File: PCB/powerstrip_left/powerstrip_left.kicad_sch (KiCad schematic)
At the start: 0 parts

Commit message: Stripe PCB's
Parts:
- added C1, C12, C13, C2: 100n, Capacitor_SMD:C_0201_0603Metric_Pad0.64x0.40mm_HandSolder, symbol Device:C
- added C10, C11, C3, C4, C5, C6, C7, C8, C9: C_Polarized, Capacitor_THT:CP_Radial_D5.0mm_P2.50mm, symbol Device:C_Polarized
- added C14: 1u, Capacitor_SMD:C_1206_3216Metric_Pad1.33x1.80mm_HandSolder, symbol Device:C
- added C15: 10u Tantal, Capacitor_SMD:C_1206_3216Metric_Pad1.33x1.80mm_HandSolder, symbol Device:C
- added IC1: PCA9685PW_Q900,118, Power_Strip_Library:SOP65P640X110-28N, symbol Power_Strip_Library:PCA9685PW_Q900,118
- added J1: XT60PW-M, Power_Strip_Library:AMASS_XT60PW-M, symbol Power_Strip_Library:XT60PW-M
- added J2, J3, J4: Conn_01x06_Pin, Connector_PinHeader_2.54mm:PinHeader_1x06_P2.54mm_Vertical, symbol Connector:Conn_01x06_Pin
- added J5, J6, J7: Conn_01x03_Pin, Connector_PinHeader_2.54mm:PinHeader_1x03_P2.54mm_Vertical, symbol Connector:Conn_01x03_Pin
- added J8: Conn_01x08_Pin, Connector_FFC-FPC:Amphenol_F32Q-1A7x1-11008_1x08-1MP_P0.5mm_Horizontal, symbol Connector:Conn_01x08_Pin
- added J9: Conn_01x02_Pin, Connector_JST:JST_XH_B2B-XH-AM_1x02_P2.50mm_Vertical, symbol Connector:Conn_01x02_Pin
- added U1: MUX508IDR, Power_Strip_Library:SOIC127P600X175-16N, symbol Power_Strip_Library:MUX508IDR
- added U2: INA181, Package_TO_SOT_SMD:SOT-23-6, symbol Amplifier_Current:INA181
- added U3: LT1117CST-3.3, PCM_Package_TO_SOT_SMD_AKL:SOT-223-3_TabPin2, symbol PCM_Voltage_Regulator_AKL:LT1117CST-3.3
- added shunt_01, shunt_2, shunt_3, shunt_4, shunt_5, shunt_6, shunt_7, shunt_8: R0.005, Resistor_SMD:R_0201_0603Metric_Pad0.64x0.40mm_HandSolder, symbol Device:R
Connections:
- new net: C1.1, U1.8 (D), U2.3 (+)
- new net 3.3V: C12.2, C13.1, C15.1, C2.1, IC1.28 (VDD), U1.13 (VDD), U2.6 (V+), U3.2 (OUT)
- new net A0: J8.4 (Pin_4), U1.1 (A0)
- new net A1: J8.3 (Pin_3), U1.16 (A1)
- new net A2: J8.2 (Pin_2), U1.15 (A2)
- new net ADC INPUT: J8.8 (Pin_8), U2.1
- new net GND: C1.2, C10.2, C11.2, C12.1, C13.2, C14.2, C15.2, C2.2, C3.2, C4.2, C5.2, C6.2, C7.2, C8.2, C9.2, IC1.1 (A0), IC1.14 (VSS), IC1.2 (A1), IC1.24 (A5), IC1.3 (A2), IC1.4 (A3), IC1.5 (A4), J1.2 (-), J2.2 (Pin_2), J8.1 (Pin_1), J9.1 (Pin_1), U1.14 (GND), U1.2 (EN), U1.3 (VSS), U2.2 (GND), U2.4 (-), U2.5 (REF), U3.1, shunt_01.2, shunt_2.2, shunt_3.2, shunt_4.2, shunt_5.2, shunt_6.2, shunt_7.2, shunt_8.2
- new net GND_SERVO1: J5.1 (Pin_1), U1.4 (S1), shunt_01.1
- new net GND_SERVO2: J5.2 (Pin_2), U1.5 (S2), shunt_2.1
- new net GND_SERVO3: J5.3 (Pin_3), U1.6 (S3), shunt_3.1
- new net GND_SERVO4: J2.1 (Pin_1), U1.7 (S4), shunt_4.1
- new net GND_SERVO6: J2.3 (Pin_3), U1.12 (S5), shunt_5.1
- new net GND_SERVO7: J2.4 (Pin_4), U1.11 (S6), shunt_6.1
- new net GND_SERVO8: J2.5 (Pin_5), U1.10 (S7), shunt_7.1
- new net GND_SERVO9: J2.6 (Pin_6), U1.9 (S8), shunt_8.1
- new net PWM_SERVO1: IC1.6 (LED0), J7.1 (Pin_1)
- new net PWM_SERVO2: IC1.7 (LED1), J7.2 (Pin_2)
- new net PWM_SERVO3: IC1.8 (LED2), J7.3 (Pin_3)
- new net PWM_SERVO4: IC1.9 (LED3), J4.1 (Pin_1)
- new net PWM_SERVO5: IC1.10 (LED4), J4.2 (Pin_2)
- new net PWM_SERVO6: IC1.11 (LED5), J4.3 (Pin_3)
- new net PWM_SERVO7: IC1.12 (LED6), J4.4 (Pin_4)
- new net PWM_SERVO8: IC1.13 (LED7), J4.5 (Pin_5)
- new net PWM_SERVO9: IC1.15 (LED8), J4.6 (Pin_6)
- new net SCL: IC1.26 (SCL), J8.6 (Pin_6)
- new net SDA: IC1.27 (SDA), J8.5 (Pin_5)
- new net VCC: C10.1, C11.1, C14.1, C3.1, C4.1, C5.1, C6.1, C7.1, C8.1, C9.1, J1.1 (+), J3.1 (Pin_1), J3.2 (Pin_2), J3.3 (Pin_3), J3.4 (Pin_4), J3.5 (Pin_5), J3.6 (Pin_6), J6.1 (Pin_1), J6.2 (Pin_2), J6.3 (Pin_3), J9.2 (Pin_2), U3.3 (IN)
- new net ¬EN: IC1.23 (~{OE}), J8.7 (Pin_7)
- no-connect marks 0 -> 8

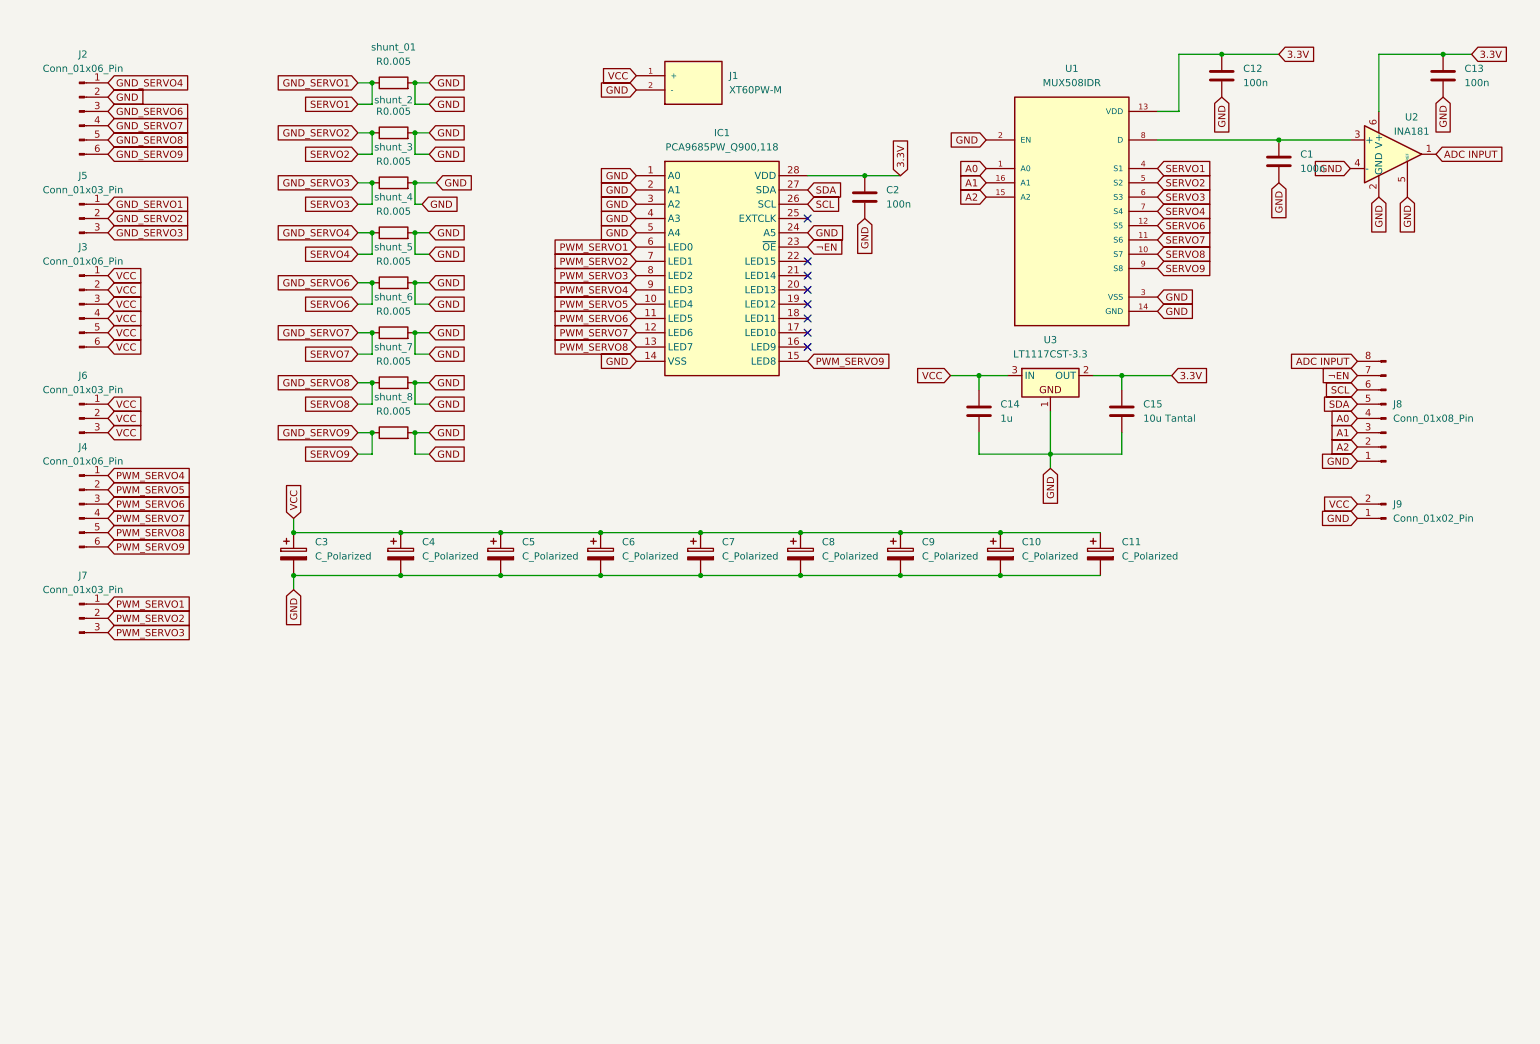
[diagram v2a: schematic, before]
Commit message: Stop tracking renders folder & final Powerstrip and Mainboard PCB
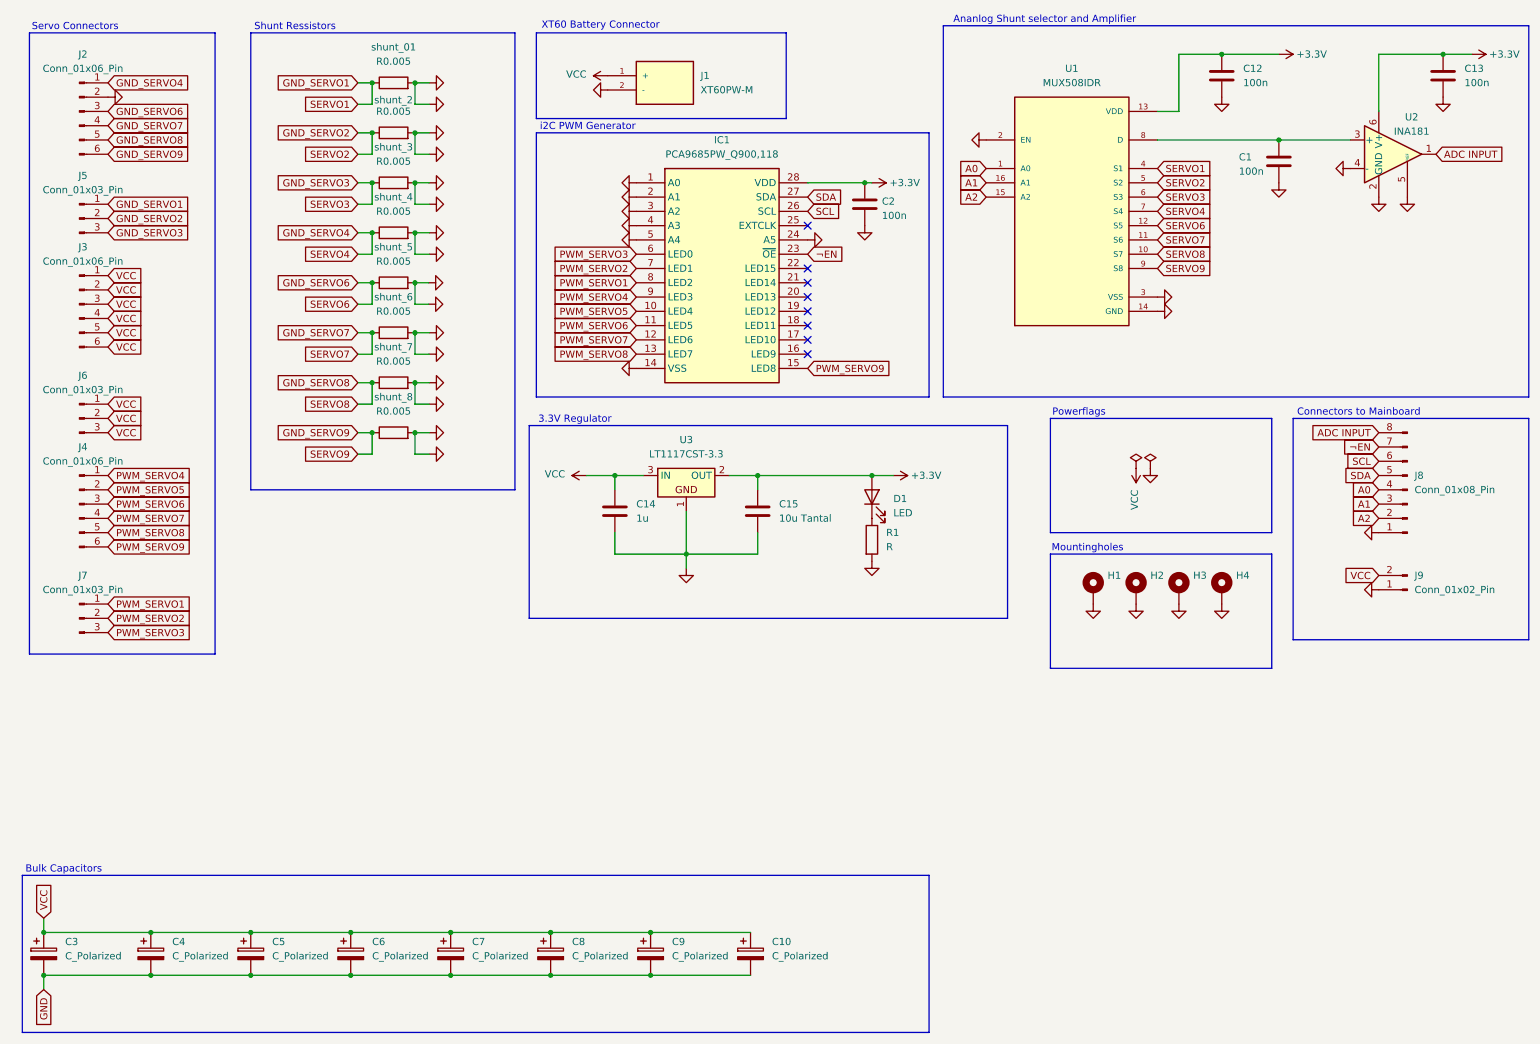
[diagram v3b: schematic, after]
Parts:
- removed C11: C_Polarized, Capacitor_THT:CP_Radial_D5.0mm_P2.50mm, symbol Device:C_Polarized
- added D1: LED, Power_Strip_Library:LEDC1608X70N, symbol Device:LED
- added H1, H2, H3, H4: MountingHole_Pad, MountingHole:MountingHole_3.5mm_Pad_Via, symbol Mechanical:MountingHole_Pad
- added R1: R, Resistor_SMD:R_0402_1005Metric_Pad0.72x0.64mm_HandSolder, symbol Device:R
- C1, C12, C13, C2: footprint Capacitor_SMD:C_0201_0603Metric_Pad0.64x0.40mm_HandSolder -> Capacitor_SMD:C_0402_1005Metric_Pad0.74x0.62mm_HandSolder
- J8: footprint Connector_FFC-FPC:Amphenol_F32Q-1A7x1-11008_1x08-1MP_P0.5mm_Horizontal -> Power_Strip_Library:17352658
- U3: footprint PCM_Package_TO_SOT_SMD_AKL:SOT-223-3_TabPin2 -> Power_Strip_Library:SOT230P700X180-4N
- shunt_01, shunt_2, shunt_3, shunt_4, shunt_5, shunt_6, shunt_7, shunt_8: footprint Resistor_SMD:R_0201_0603Metric_Pad0.64x0.40mm_HandSolder -> Resistor_SMD:R_1206_3216Metric_Pad1.30x1.75mm_HandSolder
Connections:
- net GND: now also H1.1, H2.1, H3.1, H4.1, R1.2
- net PWM_SERVO1: now also IC1.8 (LED2); no longer IC1.6 (LED0)
- net PWM_SERVO3: now also IC1.6 (LED0); no longer IC1.8 (LED2)
- net 3.3V renamed +3.3V
- net +3.3V: now also D1.2 (A)
- new net: D1.1 (K), R1.1
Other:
- note added: "3.3V Regulator"
- note added: "Ananlog Shunt selector and Amplifier"
- note added: "Bulk Capacitors"
- note added: "Connectors to Mainboard"
- note added: "Mountingholes"
- note added: "Powerflags"
- note added: "Servo Connectors"
- note added: "Shunt Ressistors"
- note added: "XT60 Battery Connector"
- note added: "i2C PWM Generator"
- moved on the sheet: C10, C14, C15, C2, C3, C4, C5, C6, C7, C8, C9, IC1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
